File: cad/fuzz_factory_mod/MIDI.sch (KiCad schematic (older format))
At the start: 14 parts, among them J901 CONN_MIDI_IN, J902 CONN_MIDI_THRU, J903 CONN_MIDI_OUT, U901 4N25, U902 4011

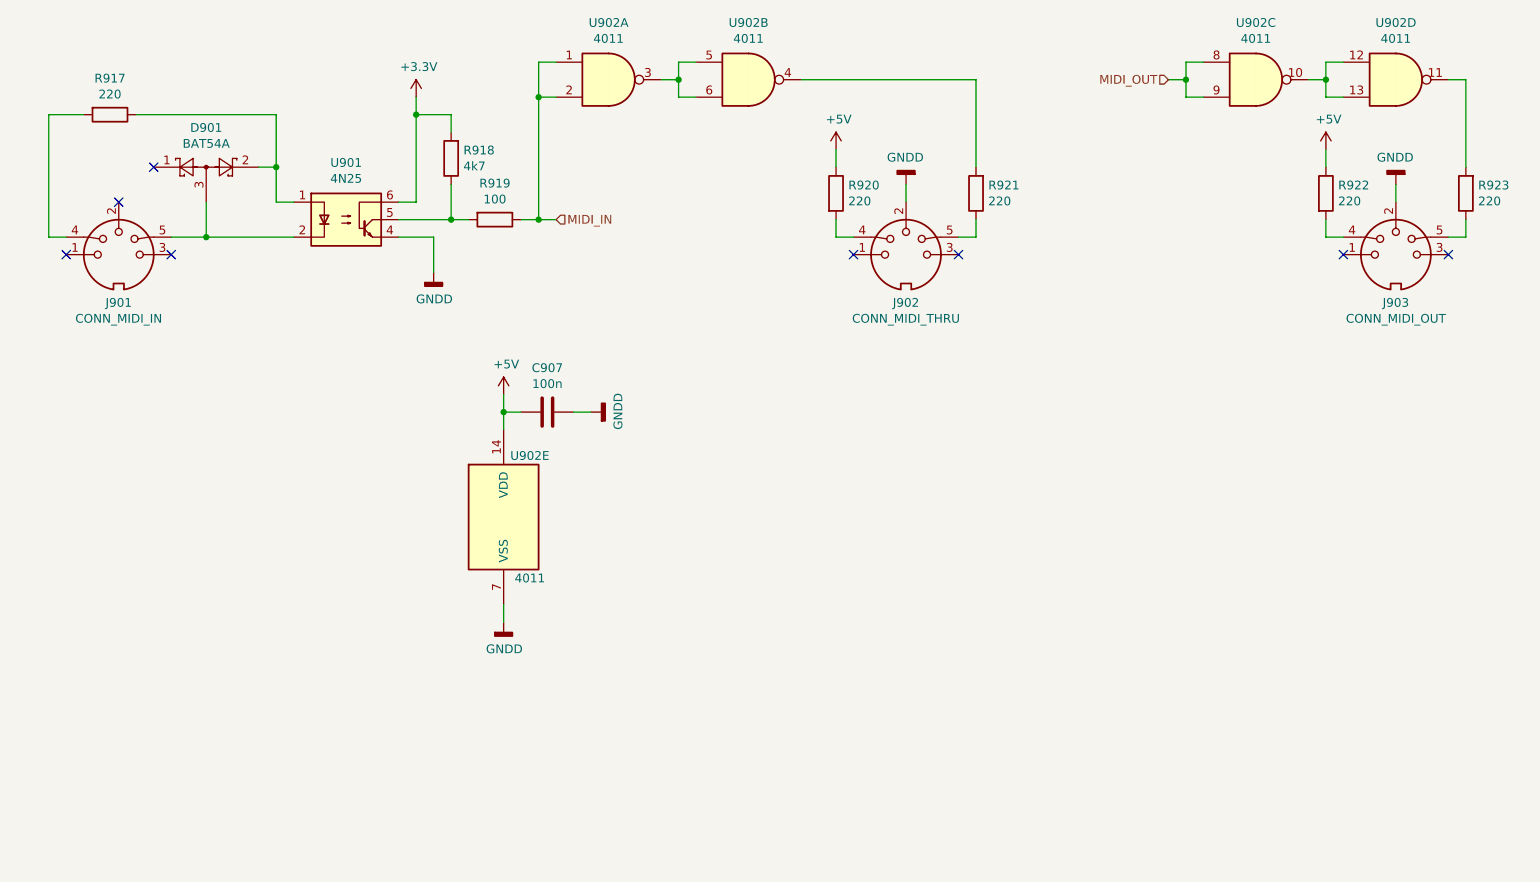
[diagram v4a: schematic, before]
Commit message: Changes architecture.
Corrections on schematic.
Continued Layout placement.
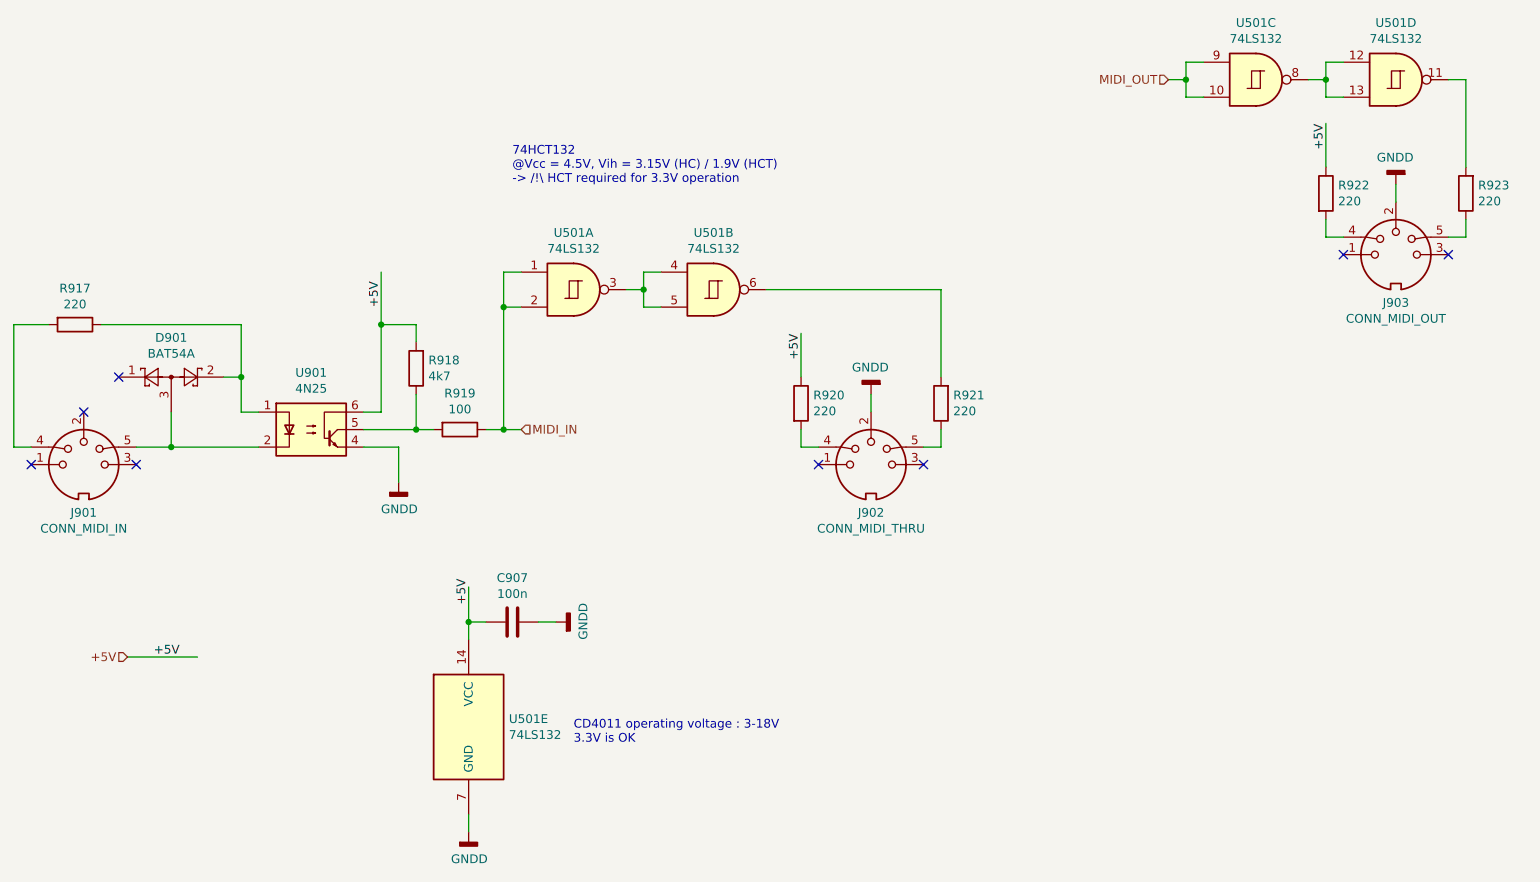
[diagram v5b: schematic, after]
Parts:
- removed U902: 4011, Housings_SOIC:SOIC-14_3.9x8.7mm_Pitch1.27mm, symbol 4xxx:4011
- added U501: 74LS132, Housings_SOIC:SOIC-14_3.9x8.7mm_Pitch1.27mm, symbol 74xx:74LS132
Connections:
- net labels removed: +3.3V
- wire segments 63 -> 64
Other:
- note added: "74HCT132\n@Vcc = 4.5V, Vih = 3.15V (HC) / 1.9V (HCT)\n-> /!\ HCT required for 3.3V operation"
- note added: "CD4011 operating voltage : 3-18V\n3.3V is OK"
- moved on the sheet: C907, D901, J901, J902, R917, R918, R919, R920, R921, U901

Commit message: Continued layout.
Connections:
- net labels added: +5V_IN
- net labels removed: +5V
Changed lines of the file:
@@
 	4800 5600 4700 5600
 Text Label 4300 5500 1    50   ~ 0
-+5V
++5V_IN
 Wire Wire Line
 	4300 5400 4300 5600
 Text Label 6200 4100 1    50   ~ 0
-+5V
++5V_IN
 Text Label 9200 2900 1    50   ~ 0
-+5V
++5V_IN
 Wire Wire Line
 	9200 2750 9200 3000
@@
 	6200 3950 6200 4200
 Text HLabel 2350 5800 0    50   Input ~ 0
-+5V
++5V_IN
 Text Label 2500 5800 0    50   ~ 0
-+5V
++5V_IN
 Wire Wire Line
 	2350 5800 2750 5800
 Text Label 3800 3800 1    50   ~ 0
-+5V
++5V_IN
 Wire Wire Line
 	3800 3600 3800 3900
